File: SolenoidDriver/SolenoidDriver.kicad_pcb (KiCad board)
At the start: 2 copper layers, 30.5 x 26 mm, 14 parts, among them J1 Conn_01x08_Pin, J2 Conn_01x08_Pin, Q1 BC818W, Q2 BC818W, Q3 BC818W, Q4 BC818W

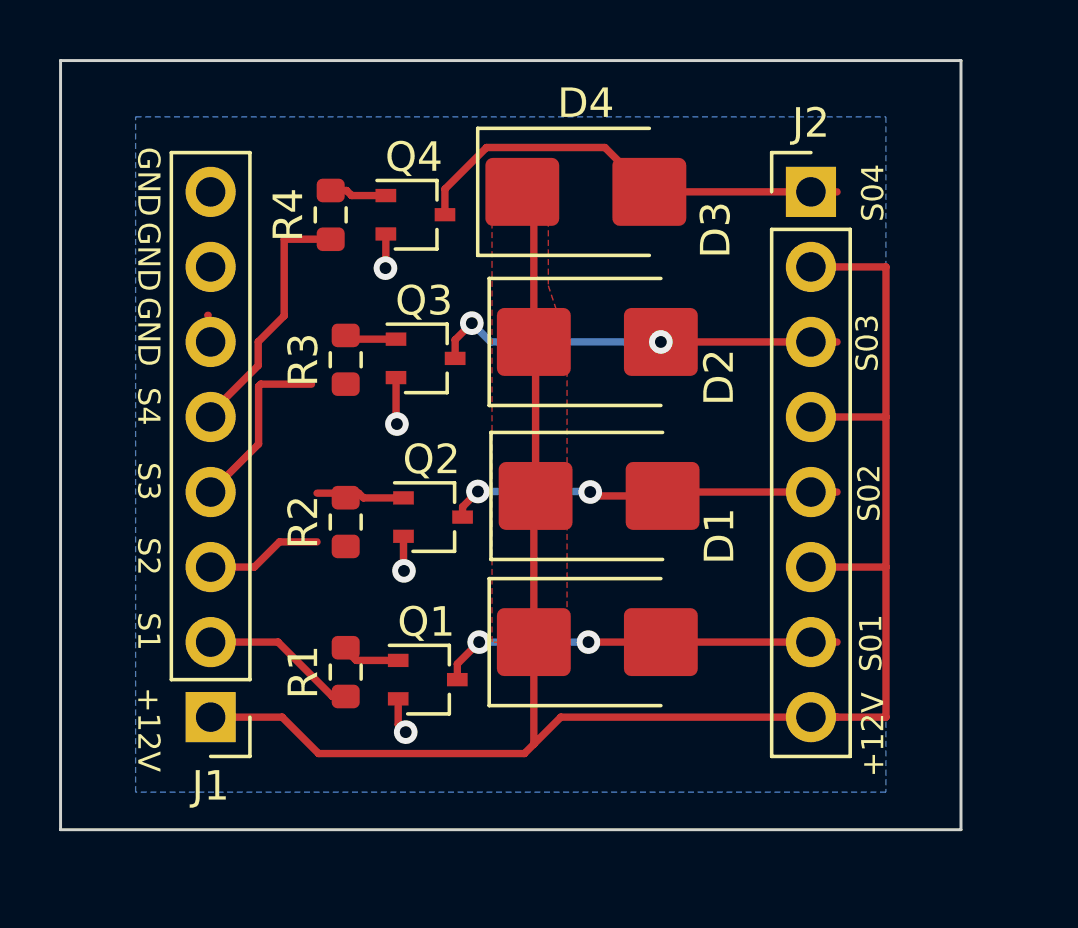
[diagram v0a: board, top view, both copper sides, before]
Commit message: Added manufacturing files for solenoid driver and 555 timer
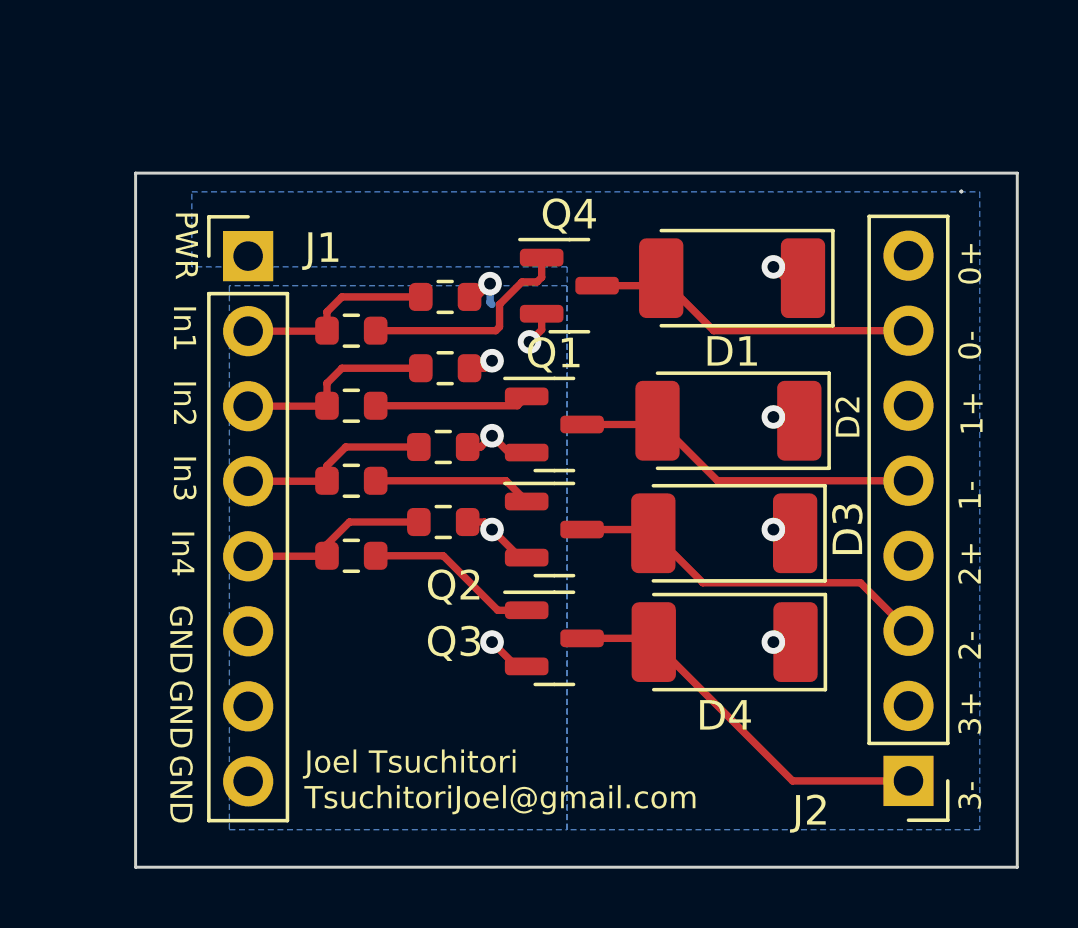
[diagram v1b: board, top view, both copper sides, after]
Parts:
- added R5: 33k, Resistor_SMD:R_0603_1608Metric, F.Cu at (87.9, 48.4)
- added R6: 33k, Resistor_SMD:R_0603_1608Metric, F.Cu at (87.9, 51.1)
- added R7: 33k, Resistor_SMD:R_0603_1608Metric, F.Cu at (87.9, 53.6)
- added R8: 33k, Resistor_SMD:R_0603_1608Metric, F.Cu at (87.9, 46.0)
- D1, D2, D3, D4: value B220 -> SM4007; footprint Diode_SMD:D_SMB -> Diode_SMD:D_MELF
- Q1, Q2, Q3, Q4: value BC818W -> 2N7002; footprint Package_TO_SOT_SMD:SOT-323_SC-70 -> Package_TO_SOT_SMD:SOT-23
- moved J2 20.2 mm to (103.6, 62.4), turned to 180 degrees
- moved D4 15.9 mm to (97.4, 57.7), turned to 180 degrees
- moved J1 15.7 mm to (81.3, 44.6), turned to 0 degrees
- moved D1 13.1 mm to (97.7, 45.4), turned to 180 degrees
- moved R4 11.6 mm to (84.8, 54.8), turned to 0 degrees
- moved R1 11.6 mm to (84.8, 47.1), turned to 0 degrees
- moved Q3 10.4 mm to (91.6, 57.6)
- moved Q1 9.64 mm to (91.6, 50.3)
- moved D3 7.77 mm to (97.4, 54.0), turned to 180 degrees
- moved Q4 5.74 mm to (92.2, 45.6)
- moved D2 5.06 mm to (97.5, 50.2), turned to 180 degrees
- moved Q2 4.13 mm to (91.6, 53.9)
- moved R3 4.10 mm to (84.8, 52.2), turned to 0 degrees
- moved R2 3.94 mm to (84.8, 49.7), turned to 0 degrees
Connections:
- Q1 pad 1: Net-(Q1-B) -> Net-(Q1-G)
- Q1 pad 3: Net-(D1-A) -> Net-(D2-A)
- Q2 pad 1: Net-(Q2-B) -> Net-(Q2-G)
- Q2 pad 3: Net-(D2-A) -> Net-(D3-A)
- Q3 pad 1: Net-(Q3-B) -> Net-(Q3-G)
- Q3 pad 3: Net-(D3-A) -> Net-(D4-A)
- Q4 pad 1: Net-(Q4-B) -> Net-(Q4-G)
- Q4 pad 3: Net-(D4-A) -> Net-(D1-A)
- R1 pad 2: Net-(Q1-B) -> Net-(Q4-G)
- R2 pad 2: Net-(Q2-B) -> Net-(Q1-G)
- R3 pad 2: Net-(Q3-B) -> Net-(Q2-G)
- R4 pad 2: Net-(Q4-B) -> Net-(Q3-G)
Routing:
- net +12V: track 65.6 -> 3.63 mm, vias 0 -> 4
- net Net-(Q4-G): track 0.00 -> 7.48 mm
- net Net-(Q3-G): track 0.00 -> 5.87 mm
- net GND: track 5.17 -> 10.6 mm, vias 4 -> 6
- net Net-(Q2-G): track 0.00 -> 5.40 mm
- net Net-(Q1-G): track 0.00 -> 5.24 mm
- net Net-(Q2-B): track 2.99 -> 0.00 mm
- net Net-(J1-Pin_3): track 3.96 -> 6.82 mm
- net Net-(D1-A): track 13.7 -> 11.4 mm, vias 2 -> 0
- net Net-(D4-A): track 15.3 -> 13.0 mm
- net Net-(J1-Pin_5): track 8.62 -> 6.48 mm
- net Net-(Q4-B): track 1.94 -> 0.00 mm
- net Net-(Q1-B): track 1.87 -> 0.00 mm
- net Net-(D3-A): track 14.1 -> 12.5 mm, vias 2 -> 0
- net Net-(D2-A): track 13.4 -> 11.9 mm, vias 2 -> 0
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- added copper zone on B.Cu, net +12V
- removed copper zone on F.Cu, net +12V
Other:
- board size 30.5 x 26 mm -> 29.8 x 23.5 mm
- board text added: "0+"
- board text added: "0-"
- board text added: "1+"
- board text added: "1-"
- board text added: "2+"
- board text added: "2-"
- board text added: "3+"
- board text added: "3-"
- board text added: "In1"
- board text added: "In2"
- board text added: "In3"
- board text added: "In4"
- board text added: "Joel Tsuchitori TsuchitoriJoel@gmail.com"
- board text added: "PWR"
- board text removed: "+12V"
- board text removed: "S01"
- board text removed: "S02"
- board text removed: "S03"
- board text removed: "S04"
- board text removed: "S1"
- board text removed: "S2"
- board text removed: "S3"
- board text removed: "S4"
